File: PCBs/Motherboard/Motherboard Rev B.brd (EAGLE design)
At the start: 95.9 x 90.2 mm, 58 parts, among them J1 MOLEX_504050-0691, J2 MOLEX_504050-0491, Q1 16M, Q2 32.768k

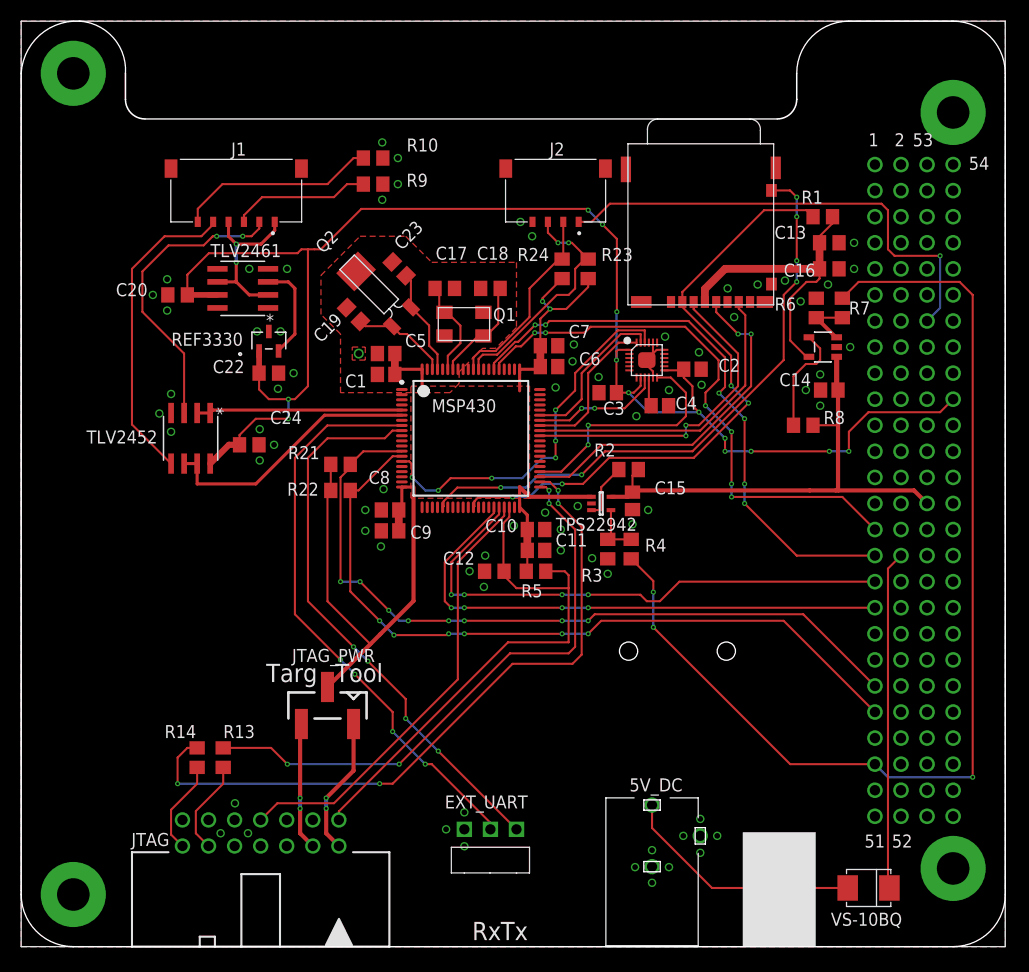
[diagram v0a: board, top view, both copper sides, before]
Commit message: Add test pads, RBF->DF13 wiring, update power distribution, breakout extra I/O pins
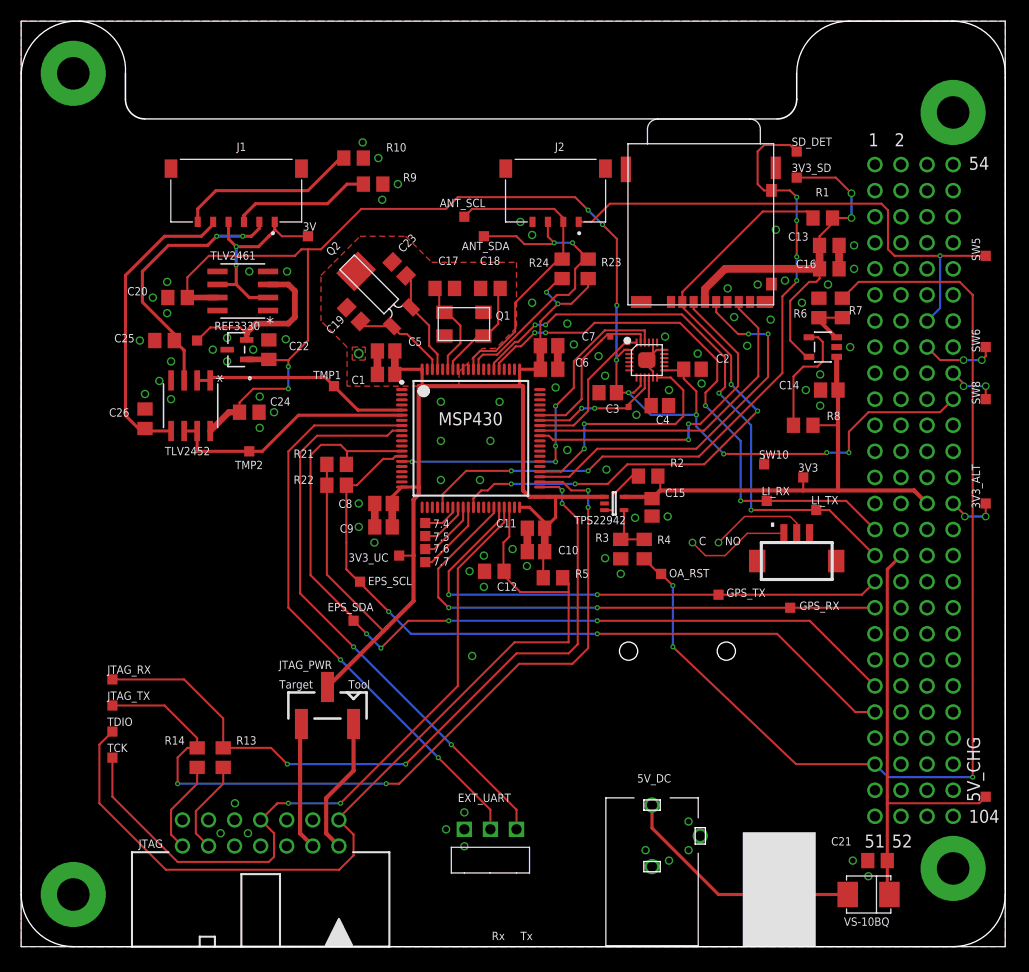
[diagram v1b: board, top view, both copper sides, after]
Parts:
- added 3V, 3V3, 3V3_ALT, 3V3_SD, 3V3_UC, 3VREF, 5V_CHG, 7.4, 7.5, 7.6, 7.7, ANT_SCL, ANT_SDA, EPS_SCL, EPS_SDA, GPS_RX, GPS_TX, JTAG_RX, JTAG_TX, LI_RX, LI_TX, OA_RST, SD_DET, SW10, SW5, SW6, SW8, TCK, TDIO, TMP1, TMP2: TPSQTP10SQ, testpad:TP10SQ
- added C21, C25, C26: 0.1uF, resistor:C0805
- added IMU_CLK, IMU_MISO, IMU_MOSI: TPSQTP06SQ, testpad:TP06SQ
- added RBF: DF13-3P-1.25V, con-hirose-df13:DF13C-3P-1.25V
- moved REF3330 3.30 mm to (21.0, 58.2), turned to 90 degrees
- moved C24 3.17 mm to (22.2, 52.1)
- moved TLV2452 3.17 mm to (16.5, 52.7)
- moved C22 2.29 mm to (24.1, 58.2), turned to 90 degrees
- moved C11 2.16 mm to (50.2, 40.8), turned to 180 degrees
- moved C10 2.16 mm to (50.2, 38.5), turned to 180 degrees
- moved C15 2.01 mm to (61.5, 42.8)
- moved R2 2.01 mm to (61.1, 45.8)
- moved R10 1.91 mm to (32.4, 76.8)
- moved R5 1.77 mm to (51.8, 35.9)
- moved R3 1.27 mm to (58.4, 38.7)
- moved R4 1.27 mm to (60.7, 38.7)
- moved TPS22942 1.27 mm to (57.8, 43.2)
- moved C8 0.90 mm to (35.3, 43.2)
- moved C9 0.74 mm to (35.3, 40.9)
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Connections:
- new net 3V3BUS2: 3V3_ALT.TP, U$1.80
- new net N$10: 7.6.TP, MSP430.29
- new net N$12: 7.7.TP, MSP430.30
- new net N$4: SW6.TP, U$1.67
- new net N$6: 7.4.TP, MSP430.27
- new net N$9: 7.5.TP, MSP430.28
- new net RBF_C: RBF.P$1
- new net RBF_NO: RBF.P$2
- new net SW8: SW8.TP, U$1.70
- net 3V: now also 3V.TP
- net 3V3: now also 3V3.TP
- net 3V3_SD: now also 3V3_SD.TP
- net 3V3_UC: now also 3V3_UC.TP
- net 3V_REF: now also 3VREF.TP
- net 5V_CHG: now also 5V_CHG.TP, C21.1
- net CLK_IMU: now also IMU_CLK.TP
- net GND: now also C21.2, C25.2, C26.2
- net JTAG_RXD: now also JTAG_RX.TP
- net JTAG_TXD: now also JTAG_TX.TP
- net LITHIUM_RX: now also LI_RX.TP
- net LITHIUM_TX: now also LI_TX.TP
- net LI_OA_RESET: now also OA_RST.TP
- net MISO_IMU: now also IMU_MISO.TP
- net MOSI_IMU: now also IMU_MOSI.TP
- net PINAVL1_RX: now also GPS_RX.TP
- net PINAVL1_TX: now also GPS_TX.TP
- net SBWTCK: now also TCK.TP
- net SBWTDIO: now also TDIO.TP
- net SCL_ANT: now also ANT_SCL.TP
- net SCL_EPS: now also EPS_SCL.TP
- net SDA_ANT: now also ANT_SDA.TP
- net SDA_EPS: now also EPS_SDA.TP
- net SD_DETECT: now also SD_DET.TP
- net SW10: now also SW10.TP
- net SW5: now also SW5.TP
- net TMP1: now also C25.1
- net TMP1_OUT: now also TMP1.TP
- net TMP2: now also C26.1
- net TMP2_OUT: now also TMP2.TP
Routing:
- net SBWTDIO: track 52.7 -> 89.7 mm
- net 3V3_UC: track 90.2 -> 124.9 mm
- net SBWTCK: track 43.5 -> 70.4 mm, vias 0 -> 2
- net JTAG_RXD: track 57.0 -> 73.2 mm
- net JTAG_TXD: track 68.5 -> 81.3 mm
- net SCL_ANT: track 19.1 -> 29.8 mm
- net 5V_CHG: track 33.0 -> 43.5 mm
- net RBF_C: track 0.00 -> 10.3 mm, vias 0 -> 1
- net SD_DETECT: track 58.6 -> 68.8 mm
- net SDA_EPS: track 74.2 -> 84.4 mm, vias 8 -> 4
- net 3V3_SD: track 30.1 -> 40.0 mm, vias 0 -> 2
- net RBF_NO: track 0.00 -> 9.94 mm, vias 0 -> 1
- net GND: track 5.15 -> 14.3 mm, vias 73 -> 84
- net SDA_ANT: track 22.9 -> 30.4 mm
- net N$12: track 0.00 -> 7.45 mm
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- removed copper zone on layer 1, net 3V3_UC
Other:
- board text added: "C"
- board text added: "NO"
- board text added: "Target"
- board text added: "VT VCC Mainboard Rev B - 8/01/18"
- board text removed: "Targ"

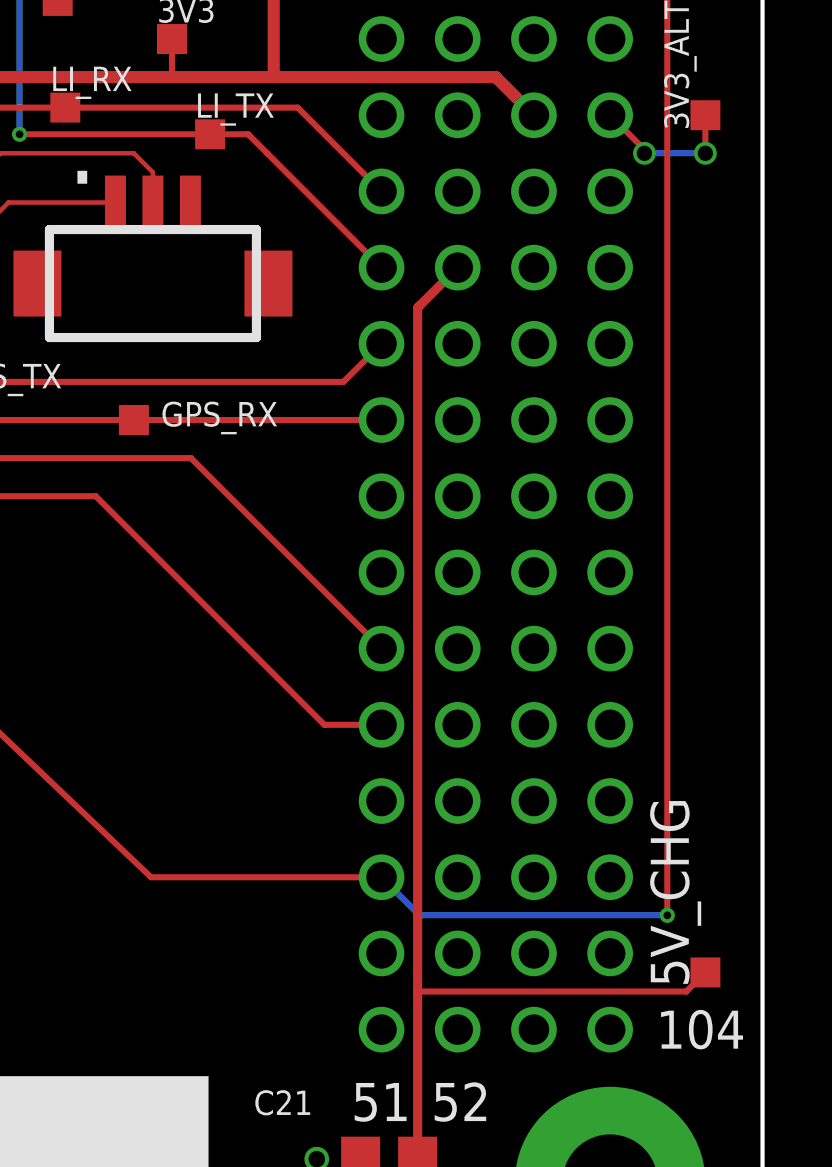
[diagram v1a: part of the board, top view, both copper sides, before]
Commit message: Add NC pin from RBF
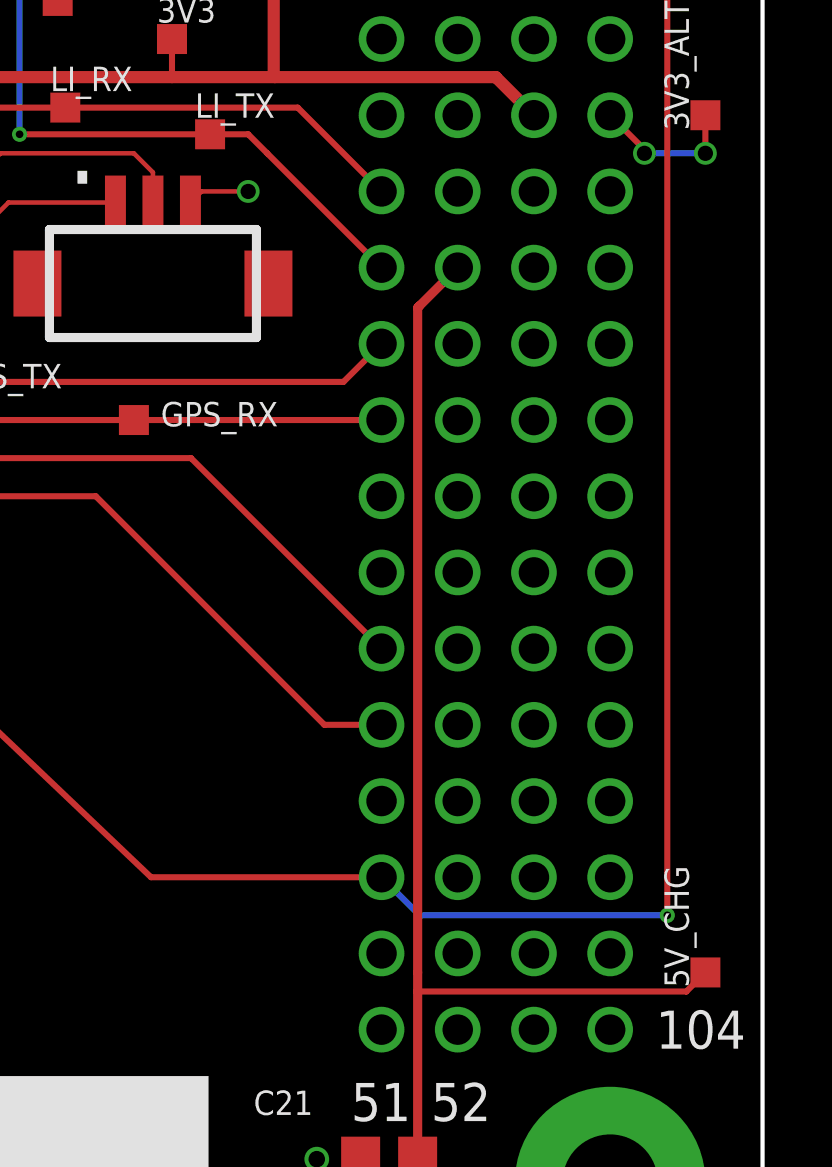
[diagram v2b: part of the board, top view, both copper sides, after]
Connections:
- new net RBF_NC: RBF.P$3
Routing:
- net RBF_NC: track 0.00 -> 2.08 mm, vias 0 -> 1
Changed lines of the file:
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@@
 </element>
 <element name="5V_CHG" library="testpad" library_urn="urn:adsk.eagle:library:385" package="TP10SQ" package3d_urn="urn:adsk.eagle:package:27962/1" value="TPSQTP10SQ" x="93.98" y="14.605" smashed="yes" rot="R90">
-<attribute name="NAME" x="93.4301" y="14.1049" size="1.27" layer="25" rot="R90"/>
+<attribute name="NAME" x="93.4301" y="14.1049" size="0.8128" layer="25" rot="R90"/>
 <attribute name="TP_SIGNAL_NAME" value="" x="95.885" y="14.605" size="1" layer="37" rot="R90"/>
 <attribute name="VALUE" x="94.615" y="14.097" size="0.0254" layer="27" rot="R90"/>
@@
 <wire x1="43.565" y1="41.025" x2="43.565" y2="42.805" width="0.2032" layer="1"/>
 </signal>
+<signal name="RBF_NC">
+<contactref element="RBF" pad="P$3"/>
+<via x="78.74" y="40.64" extent="1-16" drill="0.508"/>
+<wire x1="78.74" y1="40.64" x2="77.185" y2="40.64" width="0.1524" layer="1"/>
+<wire x1="77.185" y1="40.64" x2="76.815" y2="40.27" width="0.1524" layer="1"/>
+</signal>
 </signals>

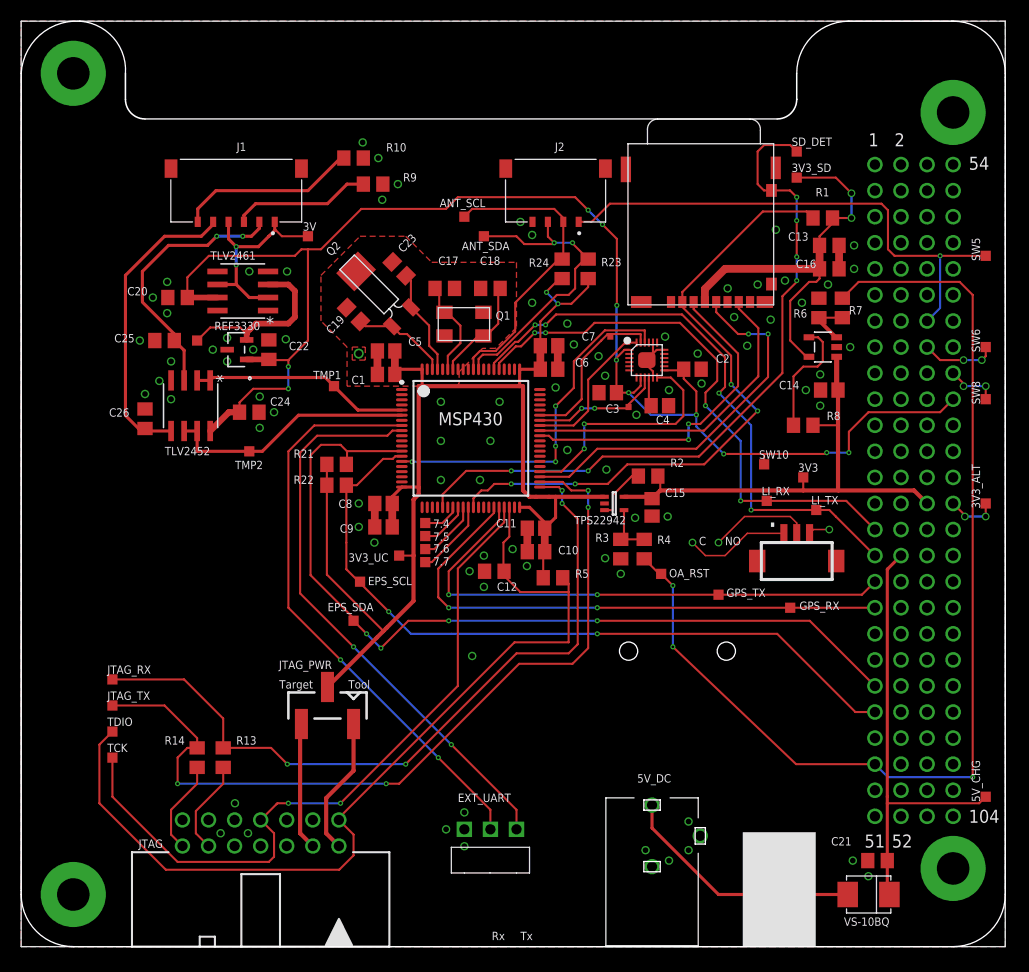
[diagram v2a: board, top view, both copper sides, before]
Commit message: Add Lithium reset pin
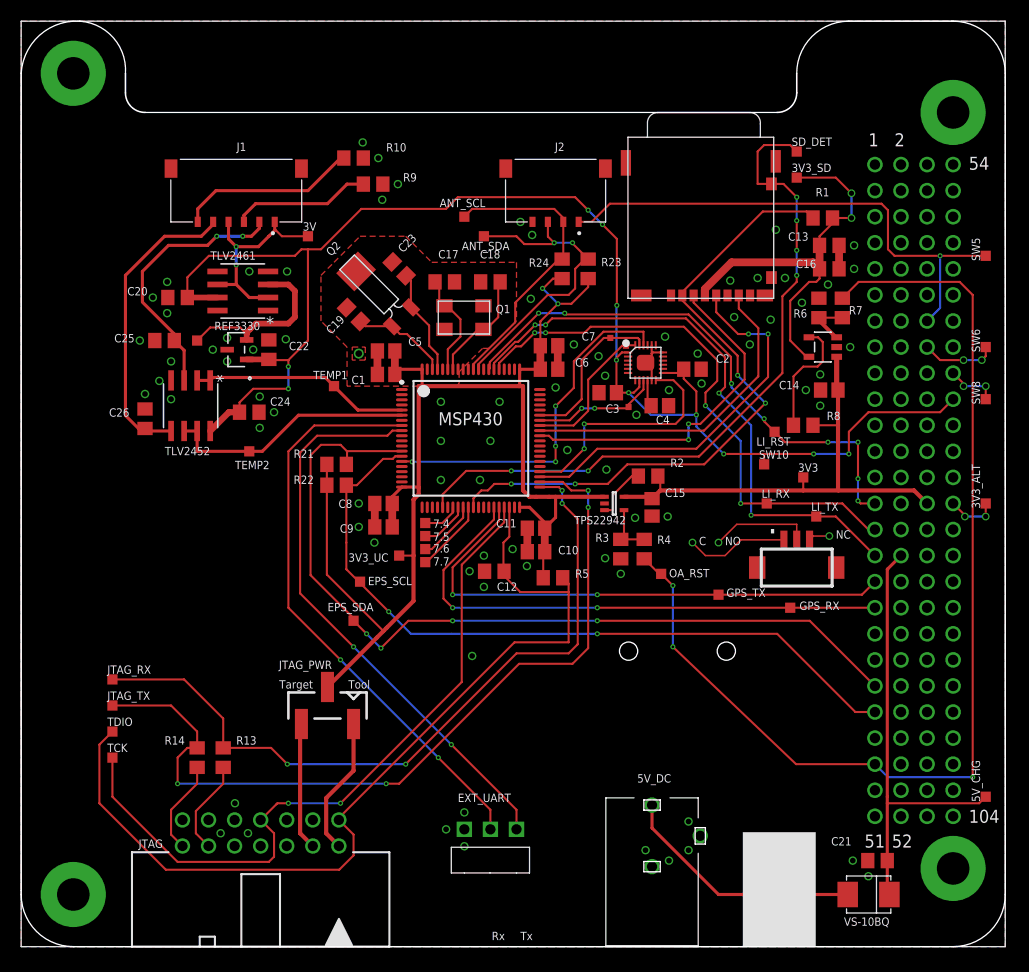
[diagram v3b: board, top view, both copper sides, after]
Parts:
- added LI_RST: TPSQTP10SQ, testpad:TP10SQ
- moved LI_TX 0.64 mm to (77.5, 41.9)
- moved SD_CONN 0.64 mm to (58.4, 62.9)
- moved Q1 0.63 mm to (40.6, 59.7)
- moved RBF 0.63 mm to (75.6, 38.7)
- moved C17 0.63 mm to (41.3, 64.8)
- moved C18 0.63 mm to (45.7, 64.8)
- moved IMU_MOSI 0.40 mm to (58.9, 58.5)
- moved U$2 0.28 mm to (60.8, 56.9)
- moved LI_RX 0.25 mm to (72.6, 43.2)
- moved IMU_CLK 0.13 mm to (57.4, 59.3)
- renumbered TMP1 to TEMP1, TMP2 to TEMP2
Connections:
- new net LITHIUM_RST: LI_RST.TP, MSP430.67, U$1.27
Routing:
- net LITHIUM_RST: track 0.00 -> 53.1 mm, vias 0 -> 8
- net MOSI_SD: track 32.5 -> 33.7 mm
- net SCL_ANT: track 29.8 -> 28.9 mm
- net CLK_IMU: track 16.5 -> 15.7 mm
- net 3V3_UC: track 124.9 -> 125.6 mm
- net PINAVL1_RX: track 54.0 -> 53.3 mm
- net MISO_SD: track 31.5 -> 32.1 mm
- net CLK_SD: track 37.4 -> 38.0 mm
- net HFXOUT: track 9.56 -> 10.2 mm
- net HFXIN: track 10.2 -> 10.9 mm
- net CS_SD: track 63.0 -> 63.6 mm
- net PINAVL1_TX: track 52.6 -> 52.1 mm
- net GND: track 14.3 -> 14.2 mm, vias 84 -> 83
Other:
- outline, holes or cut-outs redrawn
- board text added: "NC"

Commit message: Rev B final take 1
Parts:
- added GPS_PF, GPS_VPP: TPSQTP10SQ, testpad:TP10SQ
- moved EPS_SCL 49.3 mm to (80.6, 22.9)
- moved EPS_SDA 43.0 mm to (74.9, 25.4)
- moved OA_RST 26.0 mm to (80.6, 17.8)
- moved GPS_TX 6.99 mm to (74.9, 34.3)
- moved LI_RX 6.98 mm to (79.6, 43.2)
- moved GPS_RX 5.71 mm to (80.6, 33.0)
- moved ANT_SDA 0.90 mm to (45.7, 69.8)
- moved LI_TX 0.64 mm to (76.8, 41.9)
- moved 3V3_UC 0.51 mm to (36.3, 38.1)
- moved 7.4 0.51 mm to (38.9, 41.3)
- moved 7.5 0.51 mm to (38.9, 40.0)
- moved 7.6 0.51 mm to (38.9, 38.7)
- moved 7.7 0.51 mm to (38.9, 37.5)
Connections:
- net N$4 renamed SW6
- new net GPS_PF: GPS_PF.TP, MSP430.33, U$1.24
- new net GPS_VPP: GPS_VPP.TP, MSP430.34, U$1.23
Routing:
- net GPS_PF: track 0.00 -> 85.3 mm, vias 0 -> 4
- net GPS_VPP: track 0.00 -> 73.0 mm, vias 0 -> 4
- net 5V_CHG: track 43.5 -> 41.9 mm
- net SCL_EPS: track 72.1 -> 73.1 mm, vias 2 -> 4
- net SDA_ANT: track 30.1 -> 29.4 mm
- net N$9: track 4.80 -> 5.30 mm
- net N$6: track 3.62 -> 4.13 mm
- net N$12: track 7.15 -> 7.66 mm
- net N$10: track 5.97 -> 6.48 mm
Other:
- board text added: "VT VCC Mainboard Rev B - 8/02/18"
- board text removed: "VT VCC Mainboard Rev B - 8/01/18"
